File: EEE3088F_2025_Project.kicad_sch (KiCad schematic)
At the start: 46 parts, among them J1 Conn_02x16_Odd_Even, J2 USB_C_Receptacle_PowerOnly_6P, J3 Conn_01x02, Q2 NMOS, SW1 SW_SPDT, U1 HR8833, U10 INA219AIDCNR, U2 HR8833, U3 MIC2026-1YM, U4 HT7533-1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

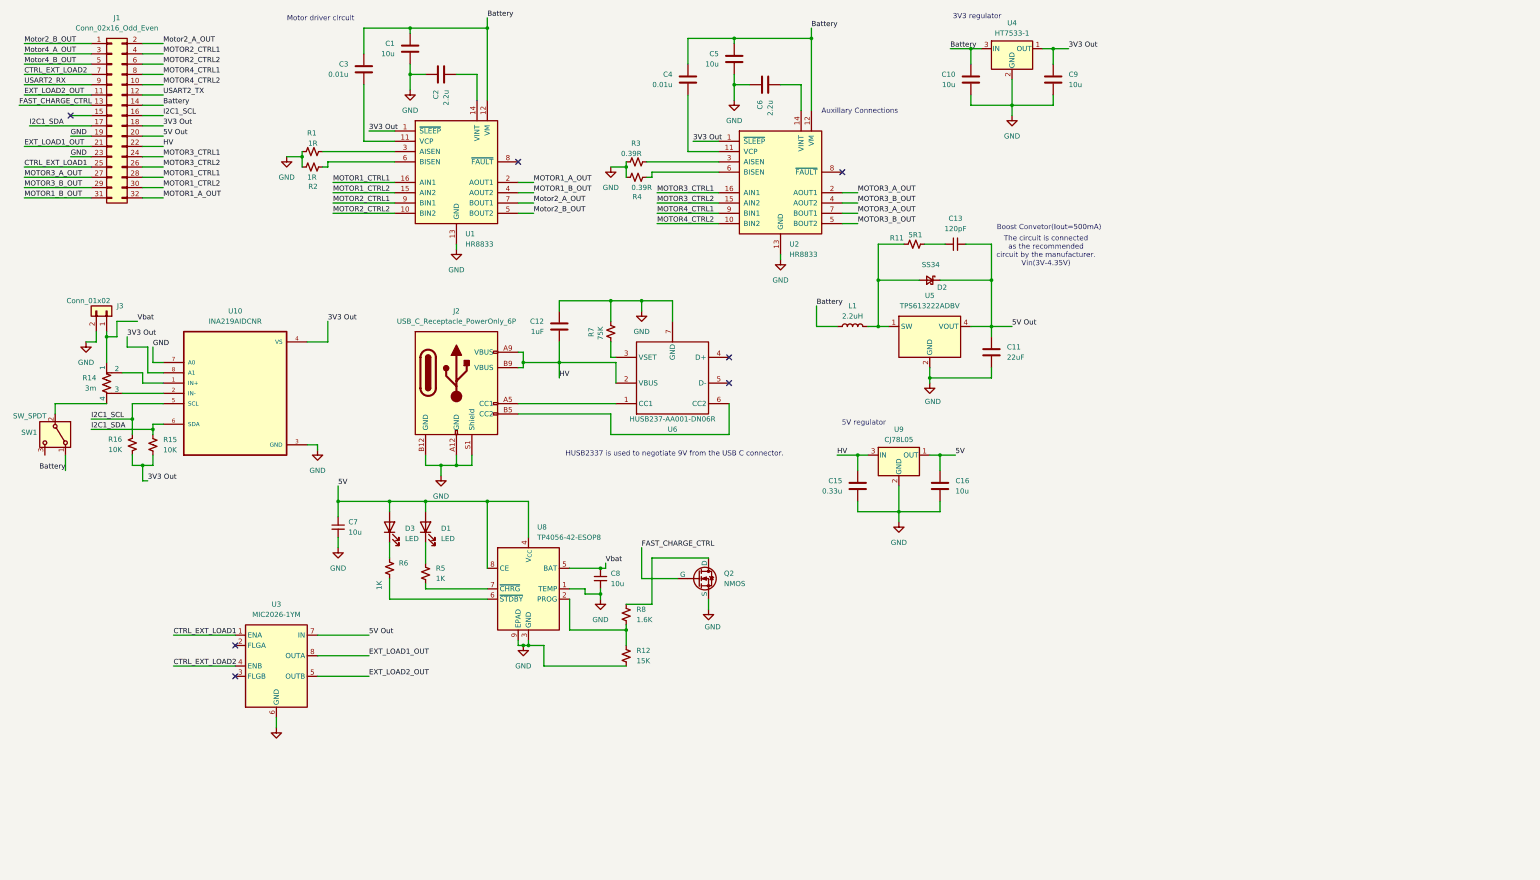
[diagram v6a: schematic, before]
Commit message: Added testpoints and board layout shape
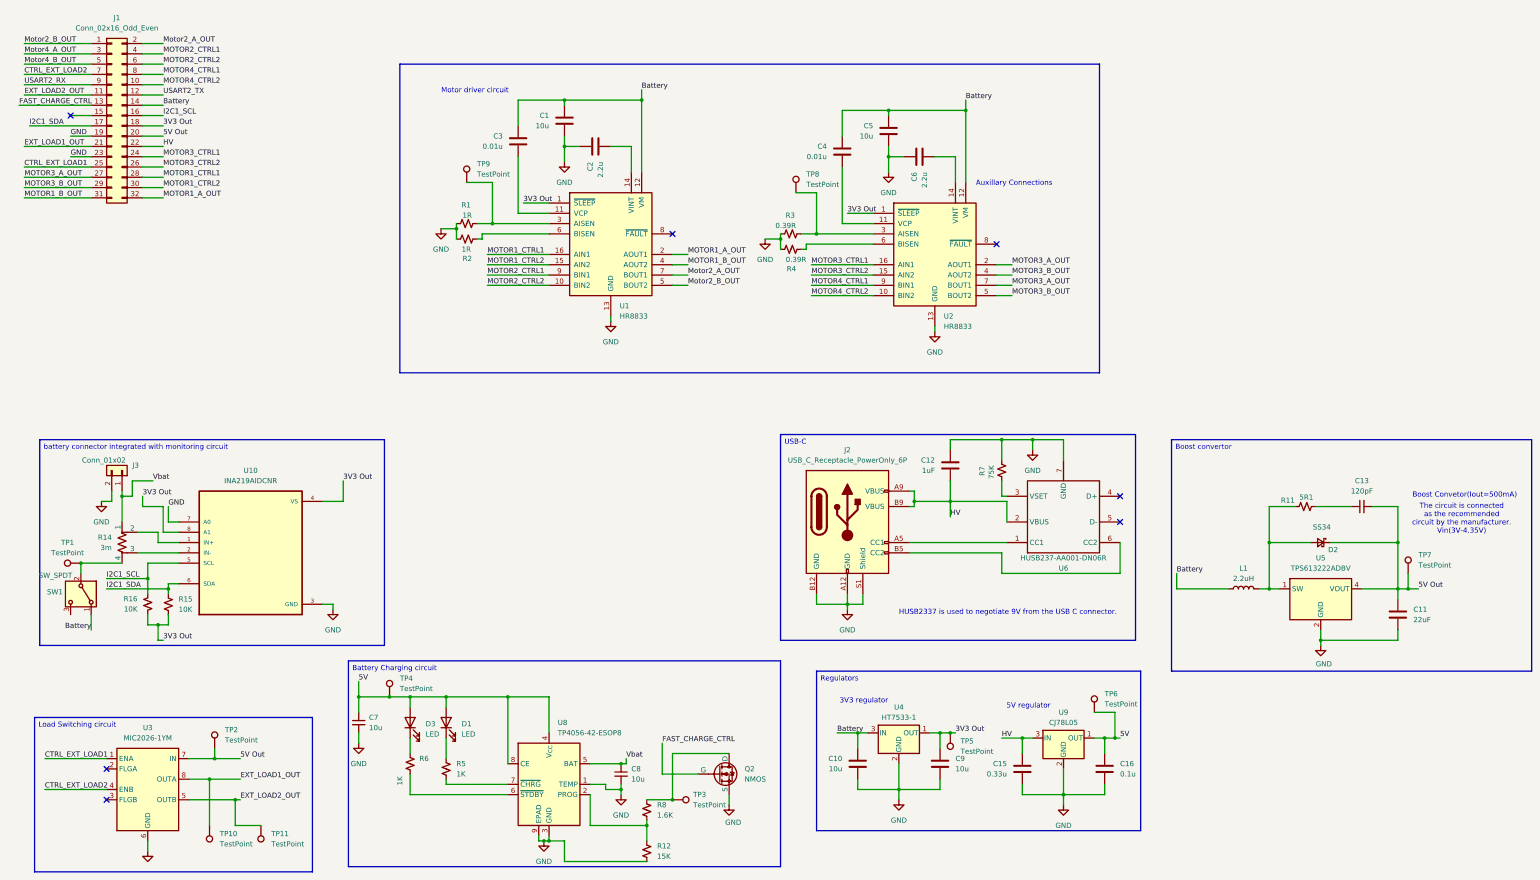
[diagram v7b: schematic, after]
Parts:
- added TP1, TP10, TP11, TP2, TP3, TP4, TP5, TP6, TP7, TP8, TP9: TestPoint, TestPoint:TestPoint_THTPad_D2.0mm_Drill1.0mm, symbol Connector:TestPoint
- C16: value 10u -> 0.1u; LCSC C3011652 -> C1525
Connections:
- net 3V3 Out: now also TP5.1
- net 5V: now also TP4.1, TP6.1
- net 5V Out: now also TP2.1, TP7.1
- net EXT_LOAD1_OUT: now also TP10.1
- net EXT_LOAD2_OUT: now also TP11.1
- net at R1.2, U1.3 (AISEN): now also TP9.1
- net at R14.4, SW1.2 (B): now also TP1.1
- net at Q2.1 (D), R8.1: now also TP3.1
- net at R3.2, U2.3 (AISEN): now also TP8.1
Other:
- moved on the sheet: C1, C10, C11, C12, C13, C15, C16, C2, C3, C4, C5, C6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

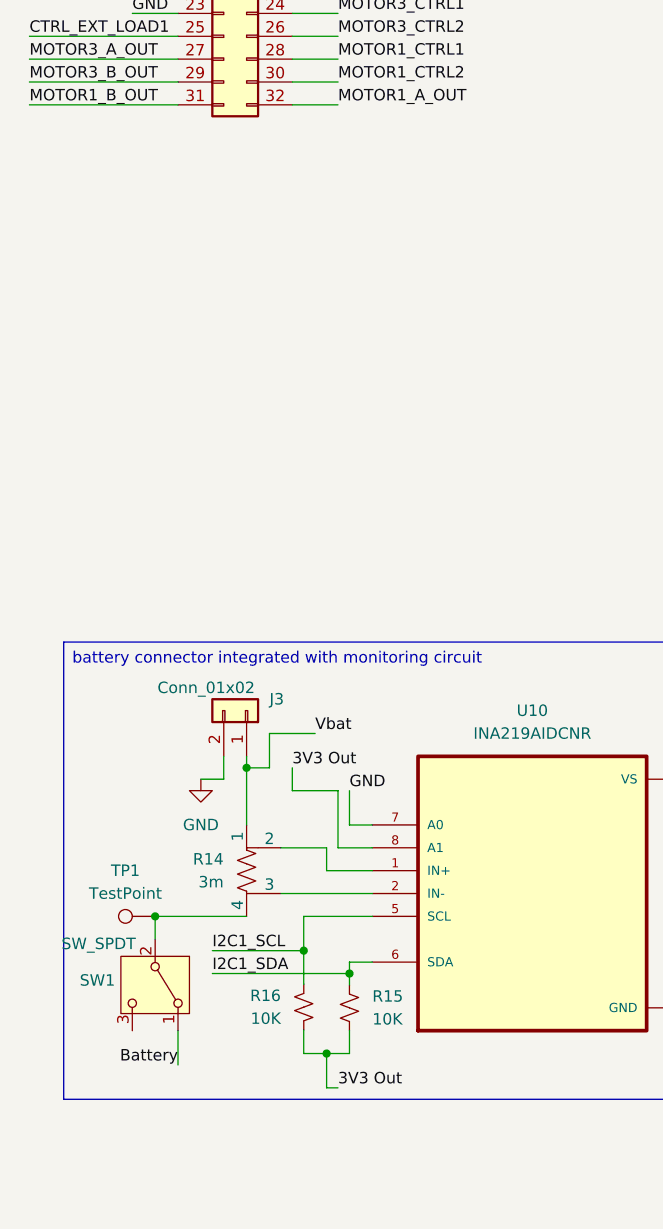
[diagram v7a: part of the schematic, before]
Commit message: Added mounting holes
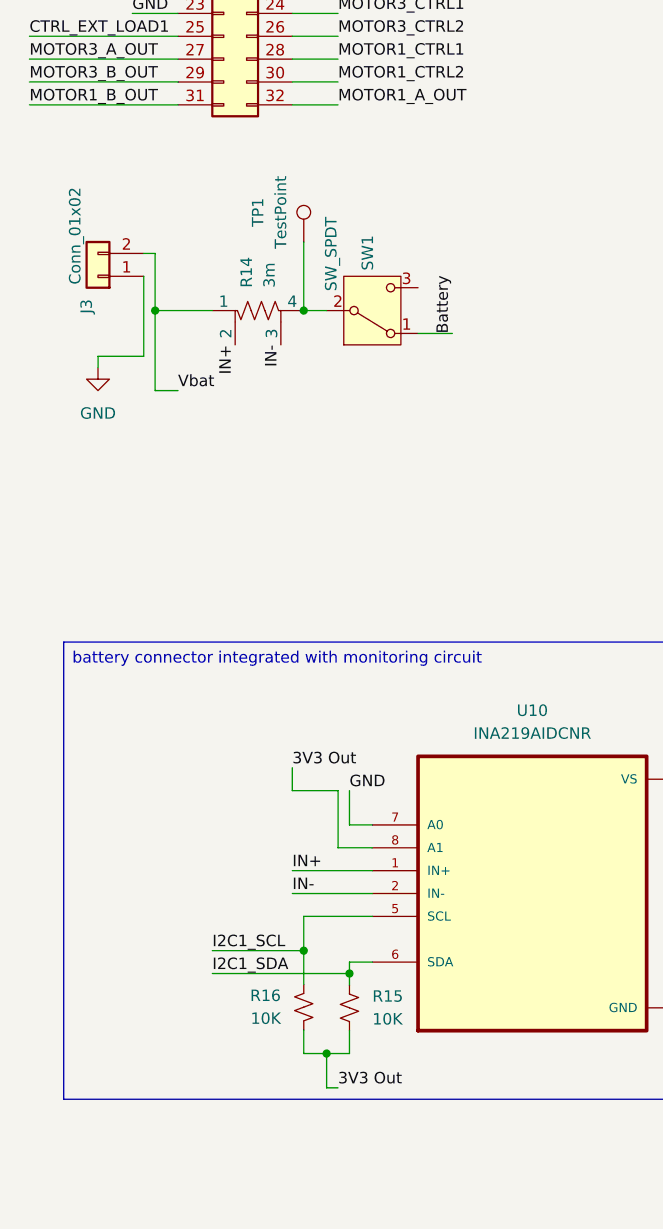
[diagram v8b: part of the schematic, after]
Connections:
- net GND: now also J3.1 (Pin_1); no longer J3.2 (Pin_2)
- net Vbat: now also J3.2 (Pin_2); no longer J3.1 (Pin_1)
- net IN+: now reaches R14.2, U10.1 (IN+)
- net IN-: now reaches R14.3, U10.2 (IN-)
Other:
- moved on the sheet: J3, R14, SW1, TP1
